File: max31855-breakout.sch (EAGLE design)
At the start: 6 parts

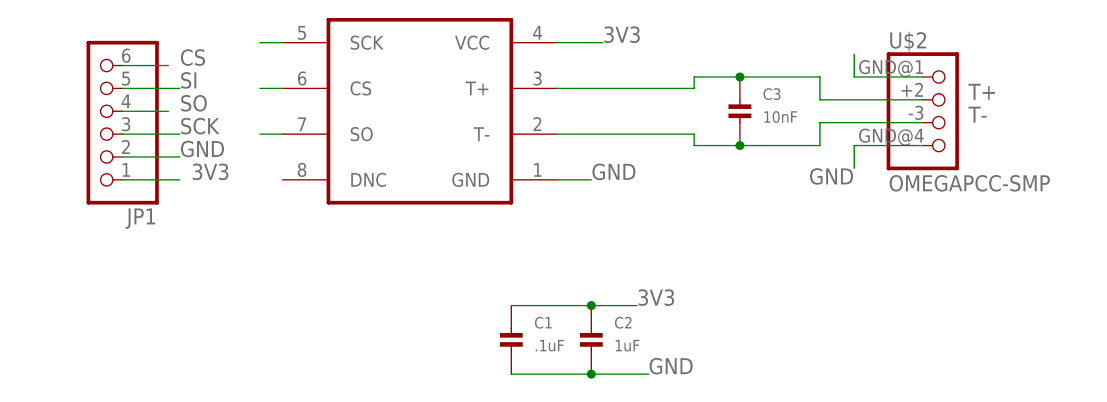
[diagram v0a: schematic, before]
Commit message: chamfer, label, add resistor jumper for use with xmega breakout - design confirmed working.
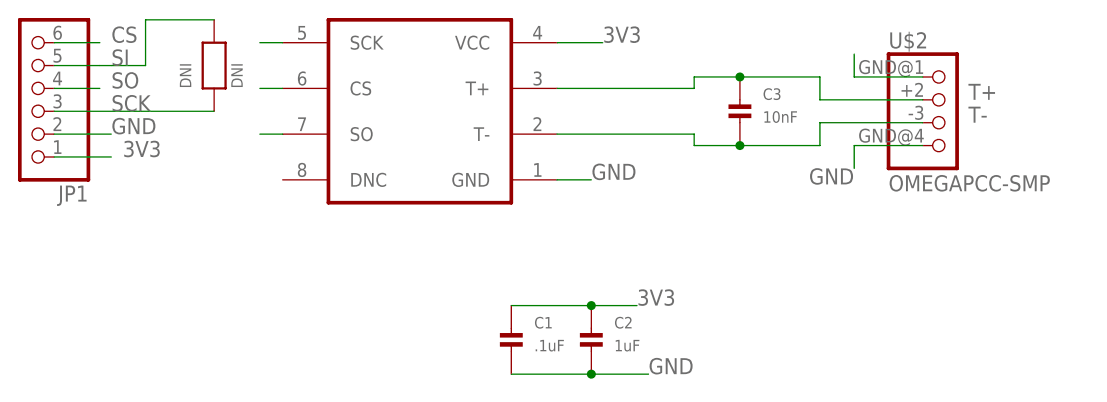
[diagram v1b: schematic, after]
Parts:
- added DNI: DNI, nonolith:RESISTOR0603
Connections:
- net SCK: now also DNI.1
- net SI: now also DNI.2
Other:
- moved on the sheet: JP1
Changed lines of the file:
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@@
 <?xml version="1.0" encoding="utf-8"?>
 <!DOCTYPE eagle SYSTEM "eagle.dtd">
-<eagle version="6.3">
+<eagle version="6.4">
 <drawing>
 <settings>
@@
 <part name="C3" library="nonolith" deviceset="CAP_CERAMIC" device="0603" value="10nF"/>
 <part name="JP1" library="nonolith" deviceset="HEADER-1X6" device="ROUND"/>
+<part name="DNI" library="nonolith" deviceset="RESISTOR" device="0603" value="DNI"/>
 </parts>
 <sheets>
@@
 <instance part="C2" gate="G$1" x="46.99" y="49.53"/>
 <instance part="C3" gate="G$1" x="63.5" y="74.93"/>
-<instance part="JP1" gate="A" x="-7.62" y="76.2" rot="R180"/>
+<instance part="JP1" gate="A" x="-15.24" y="78.74" rot="R180"/>
+<instance part="DNI" gate="G$1" x="5.08" y="81.28" rot="R90"/>
 </instances>
 <busses>
@@
 <segment>
 <pinref part="JP1" gate="A" pin="1"/>
-<wire x1="-5.08" y1="68.58" x2="1.27" y2="68.58" width="0" layer="91"/>
-<label x="2.54" y="68.58" size="1.778" layer="95"/>
+<wire x1="-12.7" y1="71.12" x2="-6.35" y2="71.12" width="0" layer="91"/>
+<label x="-5.08" y="71.12" size="1.778" layer="95"/>
 </segment>
 </net>
@@
 </segment>
 <segment>
-<label x="1.27" y="71.12" size="1.778" layer="95"/>
+<label x="-6.35" y="73.66" size="1.778" layer="95"/>
 <pinref part="JP1" gate="A" pin="2"/>
-<wire x1="-5.08" y1="71.12" x2="1.27" y2="71.12" width="0" layer="91"/>
+<wire x1="-12.7" y1="73.66" x2="-6.35" y2="73.66" width="0" layer="91"/>
 </segment>
 <segment>
@@
 </segment>
 <segment>
-<label x="1.27" y="73.66" size="1.778" layer="95"/>
+<label x="-6.35" y="76.2" size="1.778" layer="95"/>
 <pinref part="JP1" gate="A" pin="3"/>
-<wire x1="-5.08" y1="73.66" x2="1.27" y2="73.66" width="0" layer="91"/>
+<pinref part="DNI" gate="G$1" pin="1"/>
+<wire x1="-12.7" y1="76.2" x2="5.08" y2="76.2" width="0" layer="91"/>
 </segment>
 </net>
@@
 </segment>
 <segment>
-<label x="1.27" y="81.28" size="1.778" layer="95"/>
+<label x="-6.35" y="83.82" size="1.778" layer="95"/>
 <pinref part="JP1" gate="A" pin="6"/>
-<wire x1="-5.08" y1="81.28" x2="0" y2="81.28" width="0" layer="91"/>
+<wire x1="-12.7" y1="83.82" x2="-7.62" y2="83.82" width="0" layer="91"/>
 </segment>
 </net>
@@
 </segment>
 <segment>
-<label x="1.27" y="76.2" size="1.778" layer="95"/>
+<label x="-6.35" y="78.74" size="1.778" layer="95"/>
 <pinref part="JP1" gate="A" pin="4"/>
-<wire x1="-5.08" y1="76.2" x2="0" y2="76.2" width="0" layer="91"/>
+<wire x1="-12.7" y1="78.74" x2="-7.62" y2="78.74" width="0" layer="91"/>
 </segment>
 </net>
 <net name="SI" class="0">
 <segment>
-<label x="1.27" y="78.74" size="1.778" layer="95"/>
+<label x="-6.35" y="81.28" size="1.778" layer="95"/>
 <pinref part="JP1" gate="A" pin="5"/>
-<wire x1="-5.08" y1="78.74" x2="1.27" y2="78.74" width="0" layer="91"/>
-</segment>
-</net>
+<wire x1="-12.7" y1="81.28" x2="-7.62" y2="81.28" width="0" layer="91"/>
+<wire x1="-7.62" y1="81.28" x2="-6.35" y2="81.28" width="0" layer="91"/>
+<wire x1="-6.35" y1="81.28" x2="-2.54" y2="81.28" width="0" layer="91"/>
+<wire x1="-2.54" y1="81.28" x2="-2.54" y2="86.36" width="0" layer="91"/>
+<pinref part="DNI" gate="G$1" pin="2"/>
+<wire x1="-2.54" y1="86.36" x2="5.08" y2="86.36" width="0" layer="91"/>
+</segment>
+</net>
